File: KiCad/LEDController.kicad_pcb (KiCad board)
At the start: 4 copper layers, 80 x 80 mm, 79 parts, among them J1 UART, J10 LED2, J13 LED3, J14 LED4, J15 LED8, J16 LED7, J17 LED6, J18 LED5, J19 LED9, J2 VDD, J20 LED10, J21 LED11, J22 LED12, J3 GND, J6 USB_C_Receptacle_USB2.0_16P, J7 Conn_01x14, J8 JTAG, J9 LED1, K1 SRD-05VDC-SL-C, Q5 AO3400A, SW1 BOOT, SW2 EN, U1 TPS54202DDC, U2 ESP32-S3-WROOM-2, U3 TPS54202DDC, U7 SN74LVC8T245, U8 SN74LVC8T245

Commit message: arrange components
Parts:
- added C22: 100n, Capacitor_SMD:C_0805_2012Metric_Pad1.18x1.45mm_HandSolder, F.Cu at (42.0, 161.0)
- added C23: 100n, Capacitor_SMD:C_0805_2012Metric_Pad1.18x1.45mm_HandSolder, F.Cu at (36.0, 161.0)
- added C24: 100n, Capacitor_SMD:C_0805_2012Metric_Pad1.18x1.45mm_HandSolder, F.Cu at (46.5, 147.0)
- added C25: 100n, Capacitor_SMD:C_0805_2012Metric_Pad1.18x1.45mm_HandSolder, F.Cu at (52.5, 147.0)
- added D3: 1N4148WS, Diode_SMD:D_SOD-323, F.Cu at (243.5, 82.4)
- added R13: 5.1k, Resistor_SMD:R_0805_2012Metric_Pad1.20x1.40mm_HandSolder, F.Cu at (243.7, 76.5)
- added R14: 5.1k, Resistor_SMD:R_0805_2012Metric_Pad1.20x1.40mm_HandSolder, F.Cu at (243.7, 79.4)
- R5, R6: moved to F.Cu
- moved R35 186.5 mm to (32.0, 160.5), turned to 180 degrees
- moved U7 186.2 mm to (39.0, 154.0), turned to 180 degrees
- moved R41 185.0 mm to (32.0, 148.5), turned to 180 degrees
- moved U8 184.9 mm to (49.5, 154.0)
- moved R36 184.1 mm to (32.0, 158.5), turned to 180 degrees
- moved R42 182.9 mm to (32.0, 146.5), turned to 180 degrees
- moved R37 181.7 mm to (32.0, 156.5), turned to 180 degrees
- moved R38 179.5 mm to (32.0, 154.5), turned to 180 degrees
- moved R39 177.4 mm to (32.0, 152.5), turned to 180 degrees
- moved R40 175.4 mm to (32.0, 150.5), turned to 180 degrees
- moved R43 161.7 mm to (56.5, 151.0)
- moved R44 161.3 mm to (56.5, 153.0)
- moved R45 160.8 mm to (56.5, 155.0)
- moved R46 160.4 mm to (56.5, 157.0)
- moved J20 124.1 mm to (129.7, 106.7), turned to 90 degrees
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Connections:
- J10 pad 1: +24V -> +24V_SW
- J13 pad 1: +24V -> +24V_SW
- J14 pad 1: +24V -> +24V_SW
- J15 pad 1: +24V -> +24V_SW
- J16 pad 1: +24V -> +24V_SW
- J17 pad 1: +24V -> +24V_SW
- J18 pad 1: +24V -> +24V_SW
- J19 pad 1: +24V -> +24V_SW
- J20 pad 1: +24V -> +24V_SW
- J21 pad 1: +24V -> +24V_SW
- J22 pad 1: +24V -> +24V_SW
- J6 pad A4: unconnected-(J6-VBUS-PadA4) -> Net-(D3-A)
- J6 pad A5: unconnected-(J6-CC1-PadA5) -> Net-(J6-CC1)
- J6 pad A9: unconnected-(J6-VBUS-PadA4)_1 -> Net-(D3-A)
- J6 pad B4: unconnected-(J6-VBUS-PadA4)_3 -> Net-(D3-A)
- J6 pad B5: unconnected-(J6-CC2-PadB5) -> Net-(J6-CC2)
- J6 pad B9: unconnected-(J6-VBUS-PadA4)_2 -> Net-(D3-A)
- J7 pad 9: unconnected-(J7-Pin_9-Pad9) -> GPIO.18
- J9 pad 1: +24V -> +24V_SW
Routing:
- net +3.3V: track 73.3 -> 7.31 mm, vias 3 -> 0
- net ESP_BOOT: track 50.5 -> 0.00 mm, vias 3 -> 0
- net (no net): track 33.6 -> 0.00 mm, vias 1 -> 0
- net JTAG.MTMS: track 30.4 -> 0.00 mm, vias 1 -> 0
- net UART.RX: track 27.7 -> 0.00 mm, vias 1 -> 0
- net GPIO.47: track 26.6 -> 0.00 mm, vias 1 -> 0
- net Data1: track 26.3 -> 0.00 mm, vias 1 -> 0
- net GPIO.46: track 25.6 -> 0.00 mm
- net UART.TX: track 25.3 -> 0.00 mm, vias 1 -> 0
- net I^{2}C.SDA: track 24.2 -> 0.00 mm, vias 3 -> 0
- net GPIO.18: track 23.9 -> 0.00 mm, vias 1 -> 0
- net unconnected-(J7-Pin_8-Pad8): track 23.8 -> 0.00 mm, vias 1 -> 0
- net Relay_drive: track 23.6 -> 0.00 mm, vias 2 -> 0
- net GPIO.38: track 22.5 -> 0.00 mm, vias 2 -> 0
- net unconnected-(J7-Pin_4-Pad4): track 21.7 -> 0.00 mm, vias 1 -> 0
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- removed copper zone on B.Cu, net GND
- removed copper zone on F.Cu, net GND
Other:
- board size 80 x 80 mm -> 90 x 90 mm
- board text removed: "CK"
- board text removed: "DATA"
- board text removed: "DI"
- board text removed: "DO"
- board text removed: "MS"
- board text removed: "VDD"

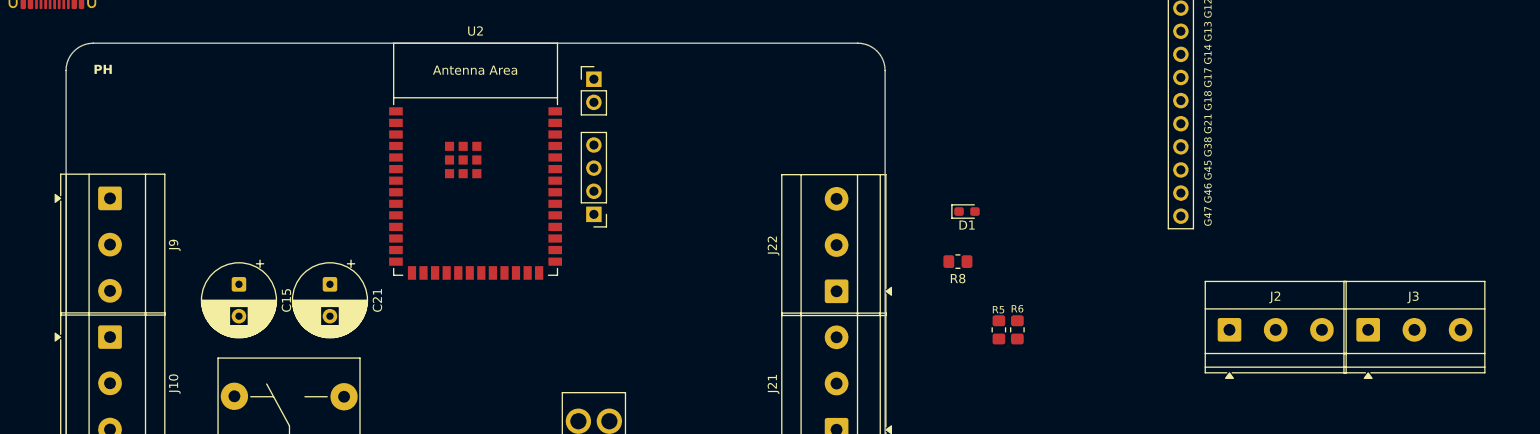
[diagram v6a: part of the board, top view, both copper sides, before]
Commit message: init agents, change schematic
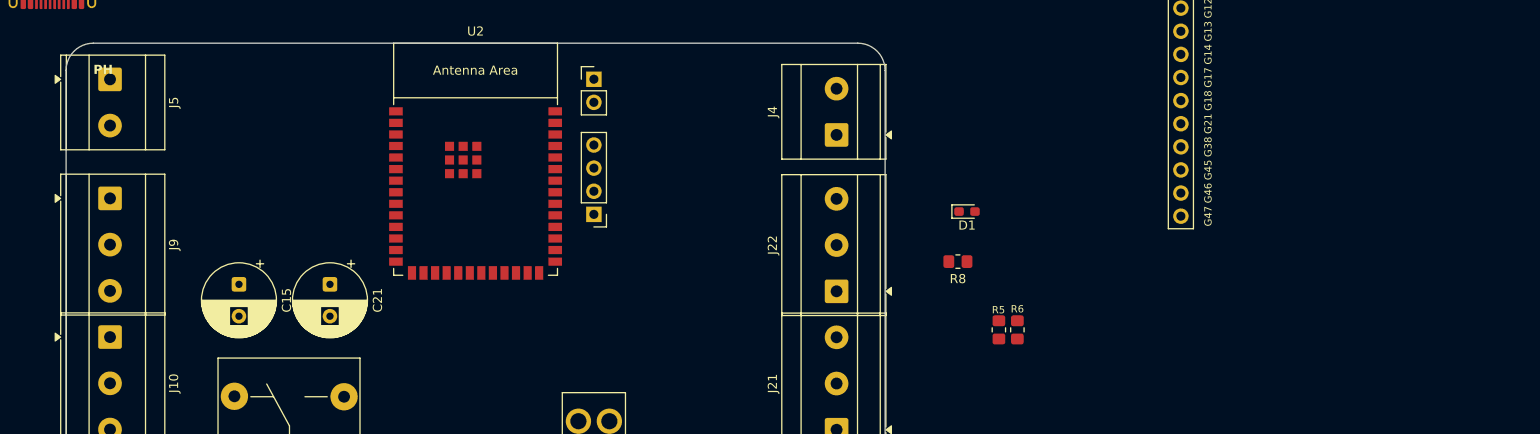
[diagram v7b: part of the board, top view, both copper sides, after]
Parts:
- removed J2: VDD, TerminalBlock_Phoenix:TerminalBlock_Phoenix_MKDS-1,5-3-5.08_1x03_P5.08mm_Horizontal
- removed J3: GND, TerminalBlock_Phoenix:TerminalBlock_Phoenix_MKDS-1,5-3-5.08_1x03_P5.08mm_Horizontal
- added J4: Conn_01x02, TerminalBlock_Phoenix:TerminalBlock_Phoenix_MKDS-3-2-5.08_1x02_P5.08mm_Horizontal, F.Cu at (129.7, 59.1)
- added J5: Conn_01x02, TerminalBlock_Phoenix:TerminalBlock_Phoenix_MKDS-3-2-5.08_1x02_P5.08mm_Horizontal, F.Cu at (49.8, 53.0)

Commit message: arrange components
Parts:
- moved F1 54.9 mm to (60.3, 64.0)
- moved SW2 53.0 mm to (75.0, 54.5)
- moved C4 49.7 mm to (77.5, 62.0), turned to 180 degrees
- moved C12 47.6 mm to (77.5, 60.0), turned to 180 degrees
- moved C3 46.7 mm to (78.5, 56.5)
- moved C2 46.5 mm to (71.0, 53.0), turned to -90 degrees
- moved C5 43.5 mm to (69.5, 57.0)
- moved SW1 41.6 mm to (103.0, 53.0)
- moved R9 38.9 mm to (68.0, 53.0), turned to -90 degrees
- moved C1 34.0 mm to (108.0, 53.0)
- moved J1 7.11 mm to (104.0, 60.0), turned to 90 degrees
- moved J8 5.39 mm to (105.0, 72.8)
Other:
- board text added: "+"
- board text added: "-"
- board text added: "D"
